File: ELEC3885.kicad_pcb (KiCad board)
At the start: 2 copper layers, 138 x 81.5 mm, 41 parts, among them J1 MicInstIn, J2 LineIn, J3 HeadPhoneOut, J4 LineOutR, J5 LineOutL, J6 Conn_01x24_Female, J7 Conn_01x24_Female, J8 Conn_01x06_Female, J9 Conn_01x05_Female, SW1 SW_Push, SW2 SW_Push, SW3 SW_Push, SW4 SW_Push, U1 AP7313, U2 SGTL5000XNLA3, U3 Teensy4.1

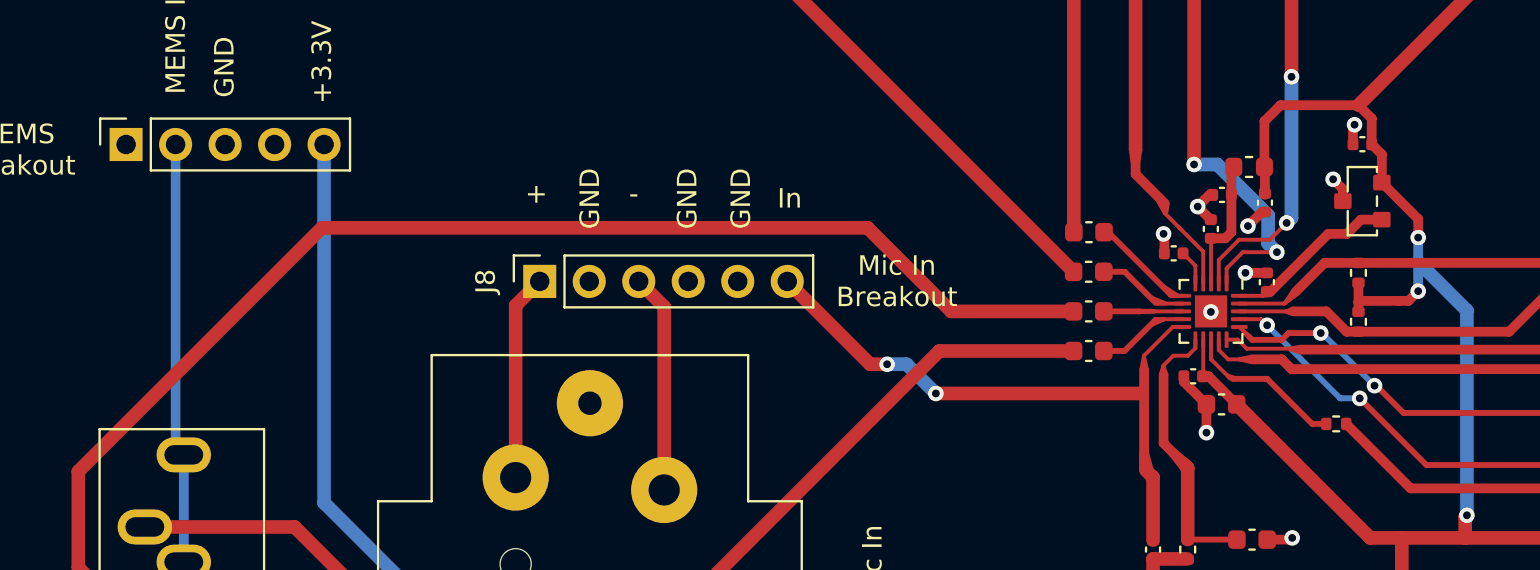
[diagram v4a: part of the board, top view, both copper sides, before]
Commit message: AP7313 Fix
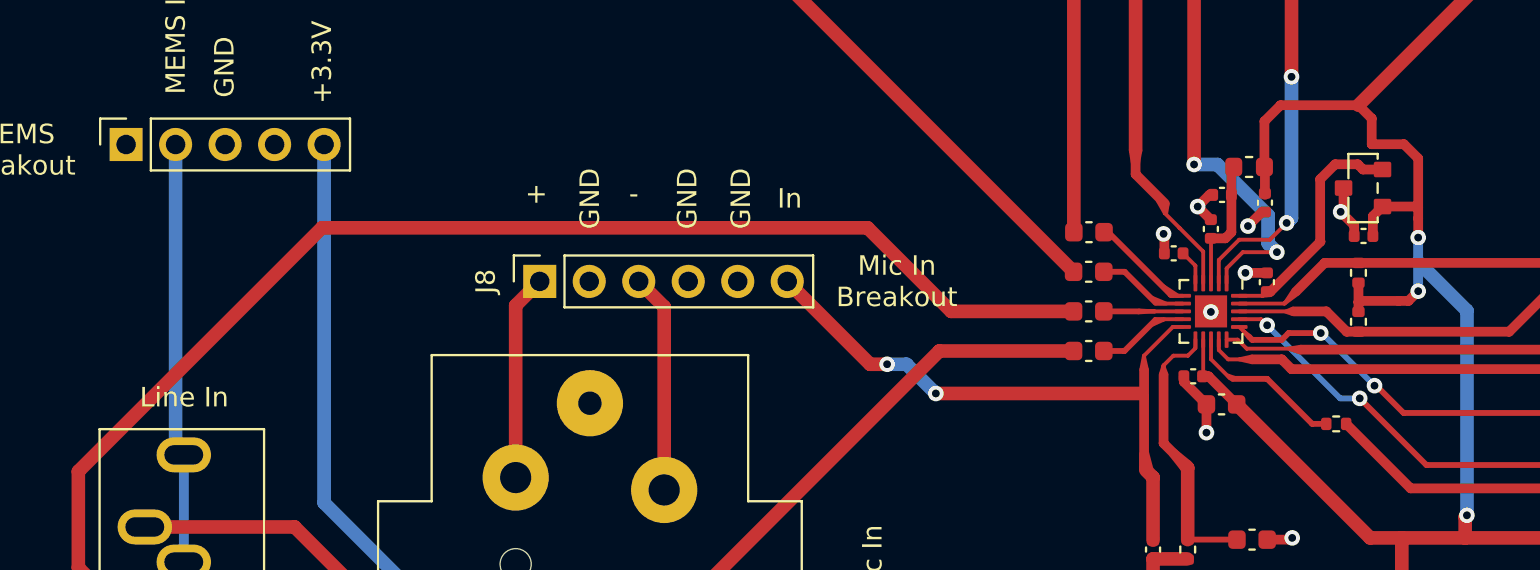
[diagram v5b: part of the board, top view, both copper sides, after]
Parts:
- moved C3 4.71 mm to (145.2, 121.4)
- moved U1 0.67 mm to (145.2, 119.0)
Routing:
- net +3.3V: track 219.0 -> 223.5 mm
- net Net-(C8-Pad1): track 8.93 -> 12.2 mm
- net GND: track 46.0 -> 46.3 mm, vias 13 -> 12
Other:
- board text added: "Line In"
